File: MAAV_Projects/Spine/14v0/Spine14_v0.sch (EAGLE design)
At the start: 101 parts, among them IC3 PINTO_SMD, J7 MA04-1, Q1 MOSFET-NCHANNELBSS138, Q3 MOSFET-NCHANNELBSS138, Q4 MOSFET-NCHANNELBSS138, Q5 32.768KHz, Q6 16MHz, Q7 CRYSTAL_16MHZ_SMD, Q8 MOSFET-NCHANNELBSS138, Q9 MOSFET-NCHANNELBSS138, U1 ATMEGA328-AU, U2 REG_3V_8SOIC

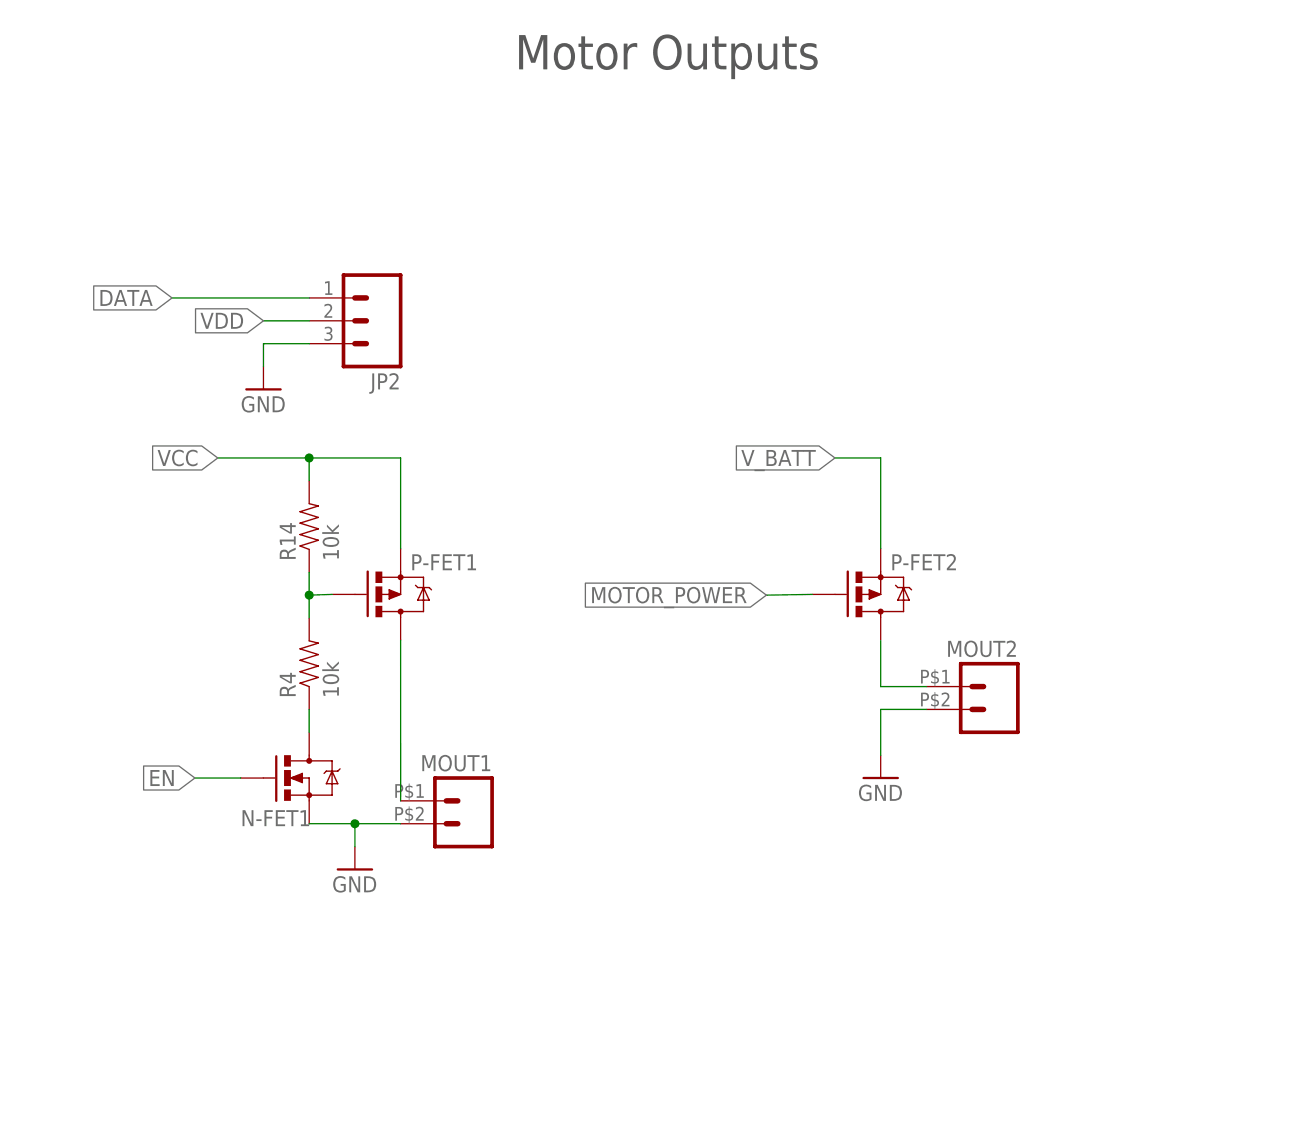
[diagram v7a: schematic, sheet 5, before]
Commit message: most level shifters, and most of motor output. only main things left are SD card and IMU
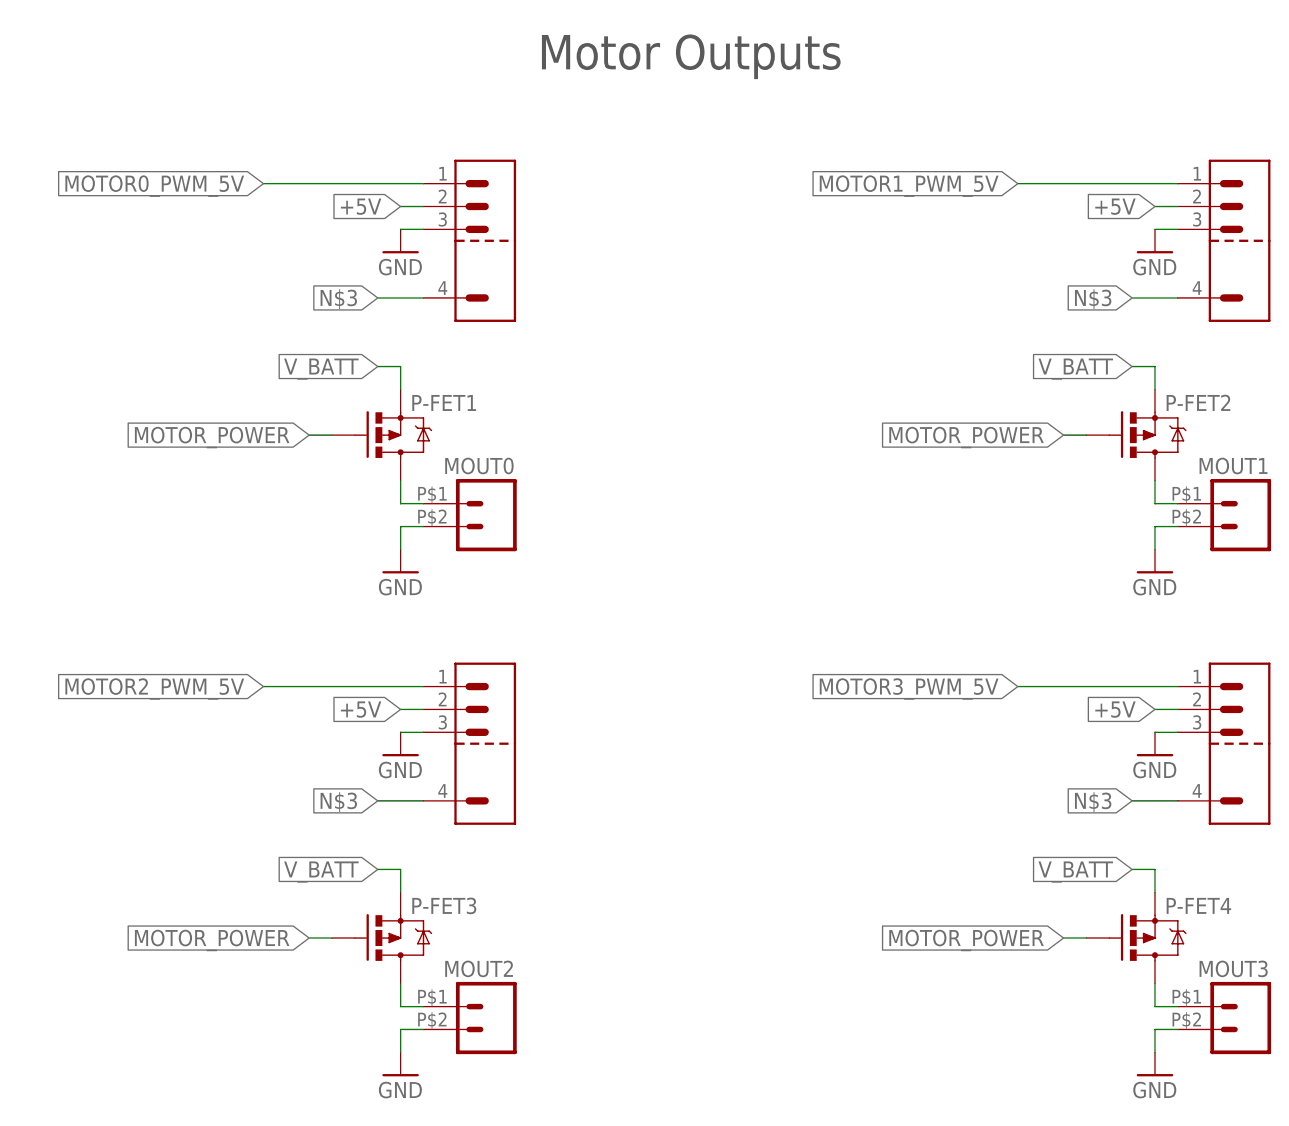
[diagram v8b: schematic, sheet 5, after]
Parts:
- removed N-FET1: MOSFET-NCHANNELBSS138, SparkFun-DiscreteSemi:MOSFET-NCHANNELBSS138
- added JP0, JP1, JP3: EDGE_LITE_CONN_HEADER_3X2_THRU_HOLE, MAAV:EDGE_LITE_CONN_HEADER_3X2_THRU_HOLE
- added MOUT0, MOUT3: MINI_FIT_JR_5569, SAUVE:MINI_FIT_JR_5569
- added P-FET3, P-FET4: MOSFET_P-CHANNEL, SAUVE:MOSFET_P-CHANNEL
- added Q10, Q11, Q12, Q13, Q14, Q2: BSS138, SparkFun-DiscreteSemi:MOSFET-NCHANNELBSS138
- added R10, R26, R27, R28, R29, R30, R31, R32, R6, R8: 10K, SparkFun:RESISTOR0603-RES
- JP2: value (none) -> EDGE_LITE_CONN_HEADER_3X2_THRU_HOLE; device SparkFun-Connectors:M03PTH -> MAAV:EDGE_LITE_CONN_HEADER_3X2_THRU_HOLE; DIGIKEY 952-2264-ND -> (none)
- R14, R4: value 10k -> 10K; device SparkFun-Resistors:RESISTOR0603-RES -> SparkFun:RESISTOR0603-RES
- renumbered U$11 to CONV
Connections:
- removed net DATA: JP2.1
- removed net EN: N-FET1.G
- removed net VCC: P-FET1.S, R14.2
- removed net VDD: JP2.2
- new net A_BATT_SENSE: R20.1, R21.2, U1.ADC6
- new net MOTOR0_PWM_5V: JP0.P$1, Q12.D, R28.2
- new net MOTOR1_PWM_5V: JP1.P$1, Q2.D, R6.2
- new net MOTOR2_PWM_5V: JP2.P$1, Q10.D, R10.2
- new net MOTOR3_PWM_5V: JP3.P$1, Q11.D, R26.2
- new net N$17: MOUT3.2, P-FET4.D
- net +1V8: now also Q10.G, Q11.G, Q12.G, Q13.G, Q14.G, Q2.G, R14.1, R27.1, R29.1, R31.1, R4.1, R8.1
- net +5V: now also JP0.P$2, JP1.P$2, JP2.P$2, JP3.P$2, R10.1, R26.1, R28.1, R30.1, R32.1, R6.1
- net GND: now also JP0.P$3, JP1.P$3, JP2.P$3, JP3.P$3, MOUT0.1, MOUT3.1; no longer JP2.3, N-FET1.S
- net MOTOR0_PWM_1V8: now also Q12.S, R27.2
- net MOTOR1_PWM_1V8: now also Q2.S, R4.2
- net MOTOR2_PWM_1V8: now also Q10.S, R8.2
- net MOTOR3_PWM_1V8: now also Q11.S, R14.2
- net MOTOR_POWER: now also P-FET1.G, P-FET3.G, P-FET4.G; no longer R20.1, R21.2, U1.ADC6
- net N$15: now also P-FET2.D; no longer P-FET1.D
- net N$16: now also MOUT2.2, P-FET3.D; no longer P-FET1.G, R14.1, R4.2
- net N$2: now also MOUT0.2, P-FET1.D; no longer N-FET1.D, R4.1
- net N$3: now also JP0.P$4, JP1.P$4, JP2.P$4, JP3.P$4; no longer MOUT2.2
- net RX1_1V8: now also Q14.S, R31.2
- net RX1_5V: now also Q14.D, R32.2
- net TX1_1V8: now also Q13.S, R29.2
- net TX1_5V: now also Q13.D, R30.2
- net V_BATT: now also P-FET1.S, P-FET3.S, P-FET4.S
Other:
- note added: "Atom to Gumstix Level Shifters"
- note added: "Gumstix Motor Level Shifters"
- note added: "Input"
- note added: "Kill Switch "Level Shifter""
- note added: "Output"
- note added: "RS-232 to UART Converter"
- note added: "Voltage Divider"
- note added: "Voltage Source"
- moved on the sheet: I2C_1, I2C_2, MOUT1, MOUT2, P-FET1, P-FET2, Q1, R1, R2, R3, SV5, U1
